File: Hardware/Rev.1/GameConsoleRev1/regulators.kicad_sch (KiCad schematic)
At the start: 13 parts, among them SW11 SW_SPDT, U4 AMS1117-3.3, U8 TLV61070ADBV

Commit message: A
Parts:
- added D11: BLUE, LED_SMD:LED_0603_1608Metric, symbol SparkFun-LED:LED
- added R49: 1k, Resistor_SMD:R_0805_2012Metric, symbol Device:R
- D10: LCSC (none) -> C965804
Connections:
- net +3V3: now also R49.2
- net GND: now also D11.1 (K)
- new net: D11.2 (A), R49.1

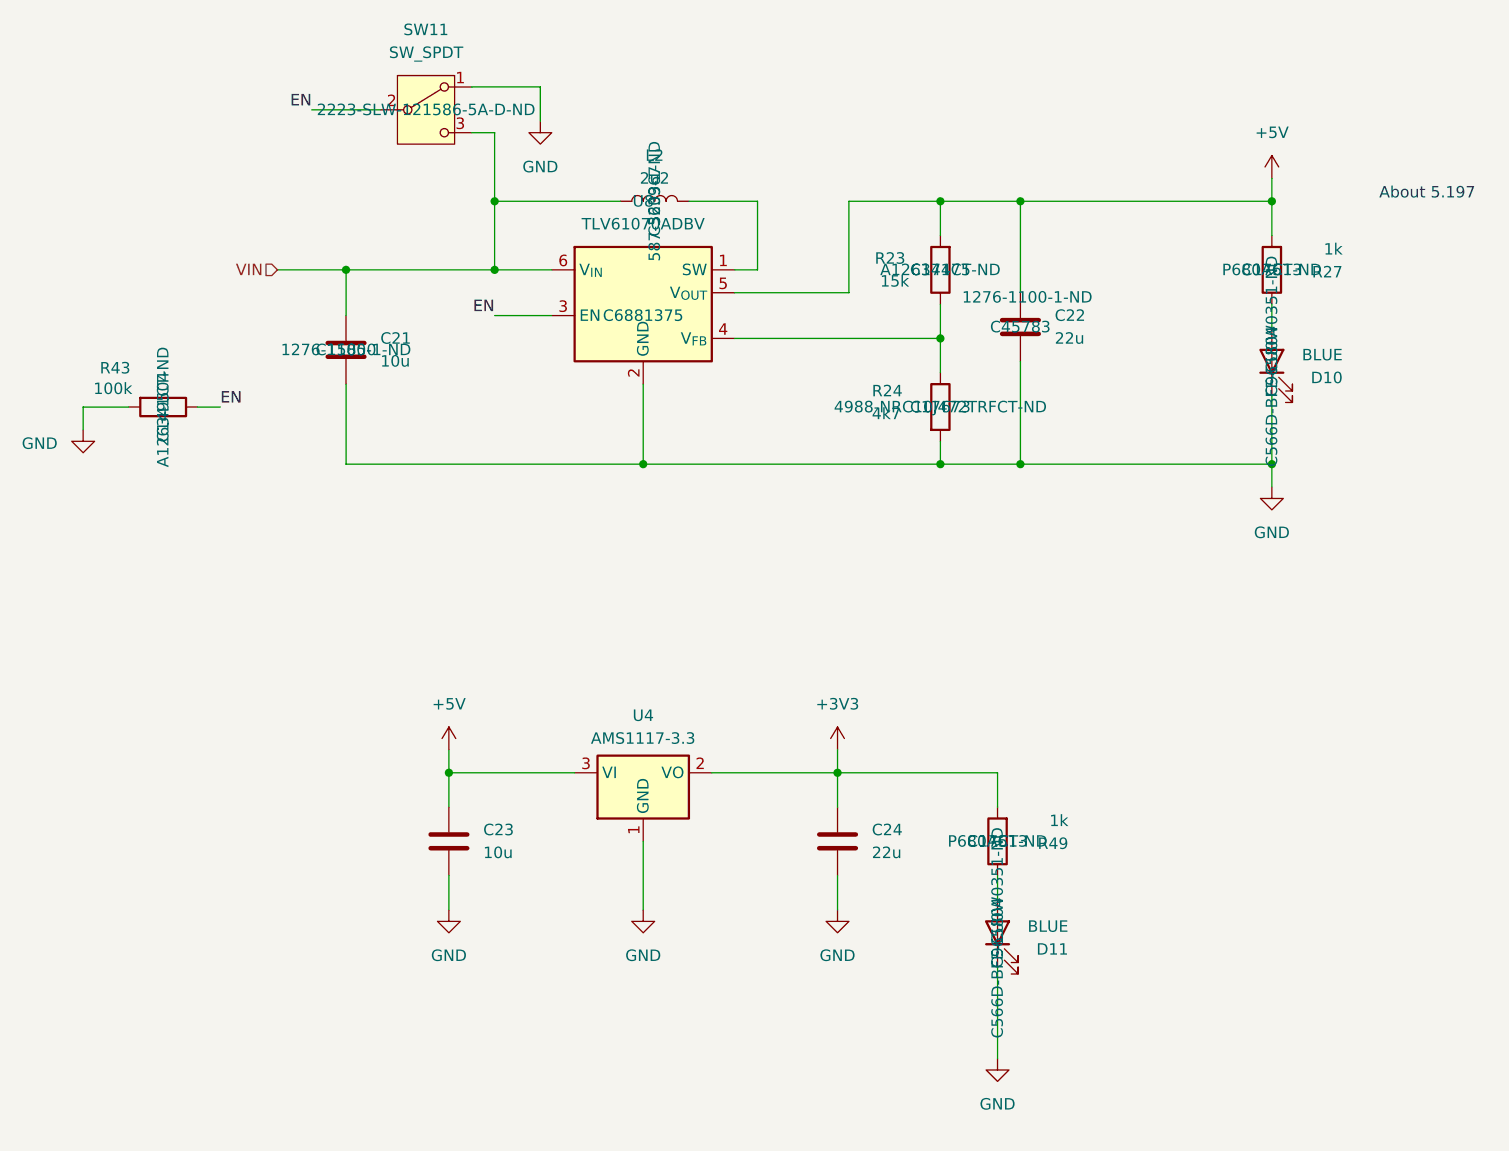
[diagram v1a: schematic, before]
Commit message: Added CPP Build
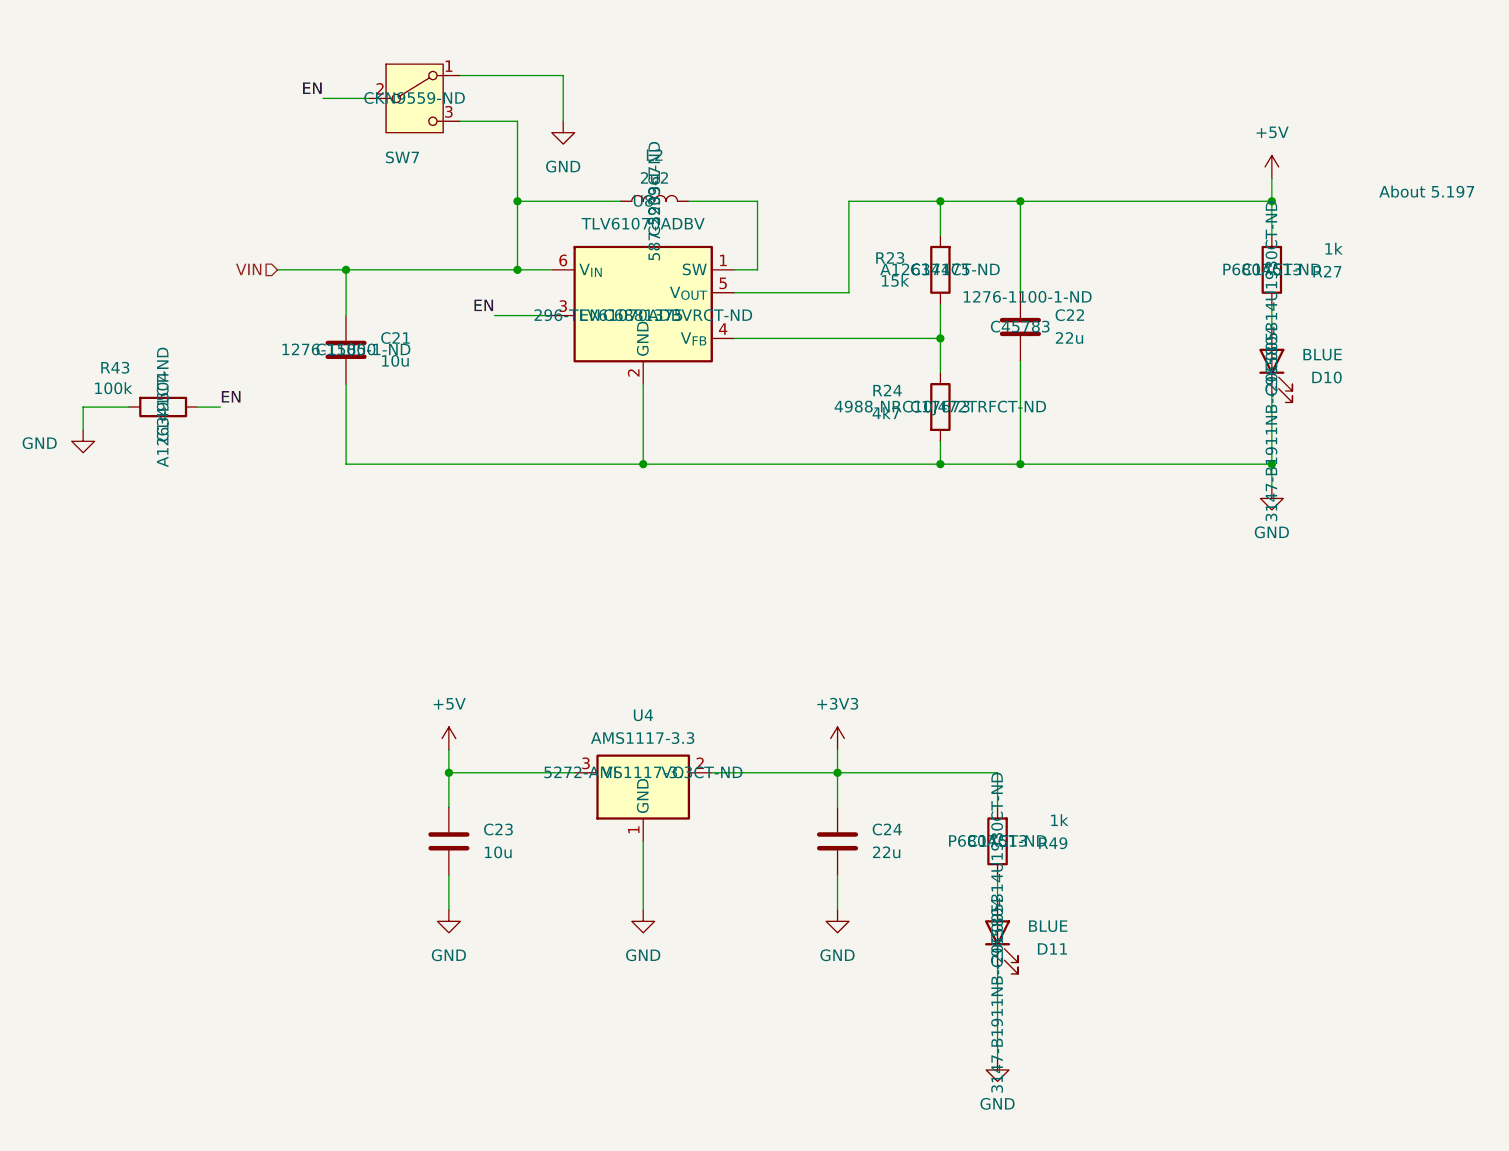
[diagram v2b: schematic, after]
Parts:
- removed SW11: SW_SPDT, AT_HUB_R2:SW_SLW-121586-5A-D, symbol Switch:SW_SPDT
- added SW7: SW_SPDT, Button_Switch_THT:SW_Slide_SPDT_Angled_CK_OS102011MA1Q, symbol Switch:SW_SPDT
- D10, D11: DK# C566D-BFE-CU0W0351-ND -> 3147-B1911NB--20C005314U1930CT-ND
- L2: DK# 587-3639-1-ND -> 587-2939-1-ND
- U4: DK# (none) -> 5272-AMS1117-3.3CT-ND
- U8: DK# (none) -> 296-TLV61070ADBVRCT-ND
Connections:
- net EN: now also SW7.2 (B)
- net GND: now also SW7.1 (A)
- net VIN: now also SW7.3 (C)
